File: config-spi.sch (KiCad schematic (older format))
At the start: 45 parts, among them J1 61300611121, U1 XC7K70T-FBG484, U3 S25FL128SAGNFI000

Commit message: Add Xilinx Platfom Cable JTAG interface
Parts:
- removed J1: 61300611121, lpddr4-test-board-footprints:61300611121, symbol lpddr4-test-board:61300611121
- removed R38, R39, R40, R41: R_100R_0402, lpddr4-test-board-footprints:0402-res, symbol lpddr4-test-board:R_100R_0402
- removed Z1, Z2, Z3, Z4: MMSZ5231B-7-F, lpddr4-test-board-footprints:SOD-123, symbol lpddr4-test-board:MMSZ5231B-7-F
- added D?: TPD6E05U06, antmicro-footprints:TPD6E05U06, symbol antmicroTVSDiodes:TPD6E05U06
- added J?: 0878311420, antmicro-footprints:PinHeader_2x7_P2mm_Drill1mm, symbol antmicroRectangularConnectorsHeadersMalePins:0878311420
- added TP?: TP_SMD1MM, lpddr4-test-board-footprints:Testpoint_smd_1mm, symbol lpddr4-test-board:TP_SMD1MM
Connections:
- net labels added: SRST_RDYN
- net labels removed: TCK, TDI_FPGA, TDO_FPGA, TMS
- wire segments 148 -> 149
- no-connect marks 1 -> 2
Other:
- note added: "Compatible with Xilinx Platform Cable"
- note added: "TODO: check this pin connection to FPGA"
- moved on the sheet: J?

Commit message: Add debug configuration resistors
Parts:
- removed JP1: MC-HVT1-S02-G, lpddr4-test-board-footprints:PinHeader_1x2_P1.27mm_Drill.7mm, symbol lpddr4-test-board:MC-HVT1-S02-G
- removed R29, R35: R_1k_0402, lpddr4-test-board-footprints:0402-res, symbol lpddr4-test-board:R_1k_0402
- removed TP?: TP_SMD1MM, lpddr4-test-board-footprints:Testpoint_smd_1mm, symbol lpddr4-test-board:TP_SMD1MM
- added R? (x5): R_1k_0402, lpddr4-test-board-footprints:0402-res, symbol lpddr4-test-board:R_1k_0402
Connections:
- net labels removed: SRST_RDYN
- wire segments 149 -> 151
- no-connect marks 2 -> 3
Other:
- note added: "Config. mode\nMaster Serial\nMaster SPI\nMaster BPI\nMaster SelectMAP\nJTAG\nSlave SelectMAP\nSlave Serial"
- note added: "Debug configuration"
- note added: "For details, see UG470 p. 21"
- note added: "MODE[2:0]\n000\n001\n010\n100\n101\n110\n111"
- note added: "Reference: UG470"
- moved on the sheet: R25

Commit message: Library cleanup, add RGMII layout
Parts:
- D4: renamed from D?; footprint antmicro-footprints:TPD6E05U06 -> lpddr4-test-board-footprints:TPD6E05U06; symbol antmicroTVSDiodes:TPD6E05U06 -> lpddr4-test-board:TPD6E05U06
- J1: renamed from J?; footprint antmicro-footprints:PinHeader_2x7_P2mm_Drill1mm -> lpddr4-test-board-footprints:PinHeader_2x7_P2mm_Drill1mm; symbol antmicroRectangularConnectorsHeadersMalePins:0878311420 -> lpddr4-test-board:0878311420
- gave numbers to parts that had none: 11
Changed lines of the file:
@@
 	11000 3700 11725 3700
 $Comp
-L lpddr4-test-board:R_200R_0402 R?
+L lpddr4-test-board:R_200R_0402 R12
 U 1 1 6AC30A74
 P 7350 8825
-F 0 "R?" H 7150 8875 60  0000 C CNN
+F 0 "R12" H 7150 8875 60  0000 C CNN
 F 1 "R_200R_0402" H 7350 8675 60  0001 C CNN
 F 2 "lpddr4-test-board-footprints:0402-res" H 7550 9025 60  0001 L CNN
@@
 $EndComp
 $Comp
-L lpddr4-test-board:R_200R_0402 R?
+L lpddr4-test-board:R_200R_0402 R11
 U 1 1 6AC310E1
 P 7350 8725
-F 0 "R?" H 7150 8775 60  0000 C CNN
+F 0 "R11" H 7150 8775 60  0000 C CNN
 F 1 "R_200R_0402" H 7350 8575 60  0001 C CNN
 F 2 "lpddr4-test-board-footprints:0402-res" H 7550 8925 60  0001 L CNN
@@
 $EndComp
 $Comp
-L lpddr4-test-board:R_200R_0402 R?
+L lpddr4-test-board:R_200R_0402 R13
 U 1 1 6AC32AC8
 P 7350 8925
-F 0 "R?" H 7150 8975 60  0000 C CNN
+F 0 "R13" H 7150 8975 60  0000 C CNN
 F 1 "R_200R_0402" H 7350 8775 60  0001 C CNN
 F 2 "lpddr4-test-board-footprints:0402-res" H 7550 9125 60  0001 L CNN
@@
 $EndComp
 $Comp
-L lpddr4-test-board:R_200R_0402 R?
+L lpddr4-test-board:R_200R_0402 R14
 U 1 1 6AC32F63
 P 7350 9025
-F 0 "R?" H 7150 9075 60  0000 C CNN
+F 0 "R14" H 7150 9075 60  0000 C CNN
 F 1 "R_200R_0402" H 7350 8875 60  0001 C CNN
 F 2 "lpddr4-test-board-footprints:0402-res" H 7550 9225 60  0001 L CNN
@@
 	6975 8825 7200 8825
 $Comp
-L lpddr4-test-board:61300411121 J?
+L lpddr4-test-board:61300411121 J8
 U 1 1 6AC614B6
 P 9425 8700
-F 0 "J?" V 9300 8675 50  0000 C CNN
+F 0 "J8" V 9300 8675 50  0000 C CNN
 F 1 "61300411121" V 9850 8700 50  0000 C CNN
 F 2 "lpddr4-test-board-footprints:PinHeader_1x4_P2.54mm_Drill1.02mm" H 9625 8900 60  0001 L CNN
@@
 $EndComp
 $Comp
-L lpddr4-test-board:61300611121 J?
+L lpddr4-test-board:61300611121 J5
 U 1 1 6AC62996
 P 6825 8725
-F 0 "J?" V 6700 8700 50  0000 C CNN
+F 0 "J5" V 6700 8700 50  0000 C CNN
 F 1 "61300611121" V 7425 8700 50  0000 C CNN
 F 2 "lpddr4-test-board-footprints:61300611121" H 7025 8925 60  0001 L CNN
@@
 	6975 9225 7250 9225
 $Comp
-L lpddr4-test-board:GND #PWR?
+L lpddr4-test-board:GND #PWR0109
 U 1 1 6B7BF2C0
 P 7250 9400
-F 0 "#PWR?" H 7250 9150 50  0001 C CNN
+F 0 "#PWR0109" H 7250 9150 50  0001 C CNN
 F 1 "GND" H 7255 9227 50  0000 C CNN
 F 2 "" H 7250 9400 50  0001 C CNN
@@
 SPI
 $Comp
-L antmicroRectangularConnectorsHeadersMalePins:0878311420 J?
+L lpddr4-test-board:0878311420 J1
 U 1 1 5FB8277B
 P 2675 8325
-F 0 "J?" H 2675 8850 50  0000 C CNN
+F 0 "J1" H 2675 8850 50  0000 C CNN
 F 1 "0878311420" H 2675 8759 50  0000 C CNN
-F 2 "antmicro-footprints:PinHeader_2x7_P2mm_Drill1mm" H 2875 8525 60  0001 L CNN
+F 2 "lpddr4-test-board-footprints:PinHeader_2x7_P2mm_Drill1mm" H 2875 8525 60  0001 L CNN
 F 3 "https://www.molex.com/pdm_docs/sd/878311420_sd.pdf" H 2875 8625 60  0001 L CNN
 F 4 "0878311420" H 2875 8825 60  0001 L CNN "MPN"
@@
 	2350 8625 2350 8800
 $Comp
-L lpddr4-test-board:GND #PWR?
+L lpddr4-test-board:GND #PWR0110
 U 1 1 5FCE9A21
 P 2350 8800
-F 0 "#PWR?" H 2350 8550 50  0001 C CNN
+F 0 "#PWR0110" H 2350 8550 50  0001 C CNN
 F 1 "GND" H 2355 8627 50  0000 C CNN
 F 2 "" H 2350 8800 50  0001 C CNN
@@
 NoConn ~ 2875 8525
 $Comp
-L antmicroTVSDiodes:TPD6E05U06 D?
+L lpddr4-test-board:TPD6E05U06 D4
 U 1 1 5FCF46CA
 P 3225 9175
-F 0 "D?" V 3445 8497 50  0000 R CNN
+F 0 "D4" V 3445 8497 50  0000 R CNN
 F 1 "TPD6E05U06" V 3354 8497 50  0000 R CNN
-F 2 "antmicro-footprints:TPD6E05U06" H 4425 9425 50  0001 C CNN
+F 2 "lpddr4-test-board-footprints:TPD6E05U06" H 4425 9425 50  0001 C CNN
 F 3 "http://www.ti.com/lit/ds/symlink/tpd6e05u06.pdf" H 4725 9525 50  0001 C CNN
 F 4 "TPD6E05U06RVZR" V 3263 8497 50  0000 R CNN "MPN"
@@
 	3775 8825 4025 8825
 $Comp
-L lpddr4-test-board:GND #PWR?
+L lpddr4-test-board:GND #PWR0111
 U 1 1 5FD74251
 P 4025 8825
-F 0 "#PWR?" H 4025 8575 50  0001 C CNN
+F 0 "#PWR0111" H 4025 8575 50  0001 C CNN
 F 1 "GND" H 4030 8652 50  0000 C CNN
 F 2 "" H 4025 8825 50  0001 C CNN
@@
 Reference: UG470
 $Comp
-L lpddr4-test-board:R_1k_0402 R?
+L lpddr4-test-board:R_1k_0402 R29
 U 1 1 60067D6F
 P 12800 7225
-F 0 "R?" H 12800 7150 60  0000 L CNN
+F 0 "R29" H 12800 7150 60  0000 L CNN
 F 1 "R_1k_0402" H 12800 7075 60  0001 C CNN
 F 2 "lpddr4-test-board-footprints:0402-res" H 13000 7425 60  0001 L CNN
@@
 	12950 7025 13100 7025
 $Comp
-L lpddr4-test-board:GND #PWR?
+L lpddr4-test-board:GND #PWR0113
 U 1 1 60091BBD
 P 13100 7225
-F 0 "#PWR?" H 13100 6975 50  0001 C CNN
+F 0 "#PWR0113" H 13100 6975 50  0001 C CNN
 F 1 "GND" H 13105 7052 50  0000 C CNN
 F 2 "" H 13100 7225 50  0001 C CNN
@@
 	12550 7025 12650 7025
 $Comp
-L lpddr4-test-board:R_1k_0402 R?
+L lpddr4-test-board:R_1k_0402 R35
 U 1 1 600B5E20
 P 12800 7525
-F 0 "R?" H 12800 7450 60  0000 L CNN
+F 0 "R35" H 12800 7450 60  0000 L CNN
 F 1 "R_1k_0402" H 12800 7375 60  0001 C CNN
 F 2 "lpddr4-test-board-footprints:0402-res" H 13000 7725 60  0001 L CNN
@@
 VCC3v3
 $Comp
-L lpddr4-test-board:R_1k_0402 R?
+L lpddr4-test-board:R_1k_0402 R37
 U 1 1 600B5E2A
 P 12800 7725
-F 0 "R?" H 12800 7650 60  0000 L CNN
+F 0 "R37" H 12800 7650 60  0000 L CNN
 F 1 "R_1k_0402" H 12800 7575 60  0001 C CNN
 F 2 "lpddr4-test-board-footprints:0402-res" H 13000 7925 60  0001 L CNN
@@
 	12950 7525 13100 7525
 $Comp
-L lpddr4-test-board:GND #PWR?
+L lpddr4-test-board:GND #PWR0114
 U 1 1 600B5E32
 P 13100 7725
-F 0 "#PWR?" H 13100 7475 50  0001 C CNN
+F 0 "#PWR0114" H 13100 7475 50  0001 C CNN
 F 1 "GND" H 13105 7552 50  0000 C CNN
 F 2 "" H 13100 7725 50  0001 C CNN
@@
 VCC3v3
 $Comp
-L lpddr4-test-board:R_1k_0402 R?
+L lpddr4-test-board:R_1k_0402 R39
 U 1 1 600BDF4C
 P 12800 8200
-F 0 "R?" H 12800 8125 60  0000 L CNN
+F 0 "R39" H 12800 8125 60  0000 L CNN
 F 1 "R_1k_0402" H 12800 8050 60  0001 C CNN
 F 2 "lpddr4-test-board-footprints:0402-res" H 13000 8400 60  0001 L CNN
@@
 	12950 8000 13100 8000
 $Comp
-L lpddr4-test-board:GND #PWR?
+L lpddr4-test-board:GND #PWR0115
 U 1 1 600BDF54
 P 13100 8200
-F 0 "#PWR?" H 13100 7950 50  0001 C CNN
+F 0 "#PWR0115" H 13100 7950 50  0001 C CNN
 F 1 "GND" H 13105 8027 50  0000 C CNN
 F 2 "" H 13100 8200 50  0001 C CNN
@@
 MODE2
 $Comp
-L lpddr4-test-board:R_1k_0402 R?
+L lpddr4-test-board:R_1k_0402 R38
 U 1 1 600D5CDE
 P 12800 8000
-F 0 "R?" H 12800 7925 60  0000 L CNN
+F 0 "R38" H 12800 7925 60  0000 L CNN
 F 1 "R_1k_0402" H 12800 7850 60  0001 C CNN
 F 2 "lpddr4-test-board-footprints:0402-res" H 13000 8200 60  0001 L CNN

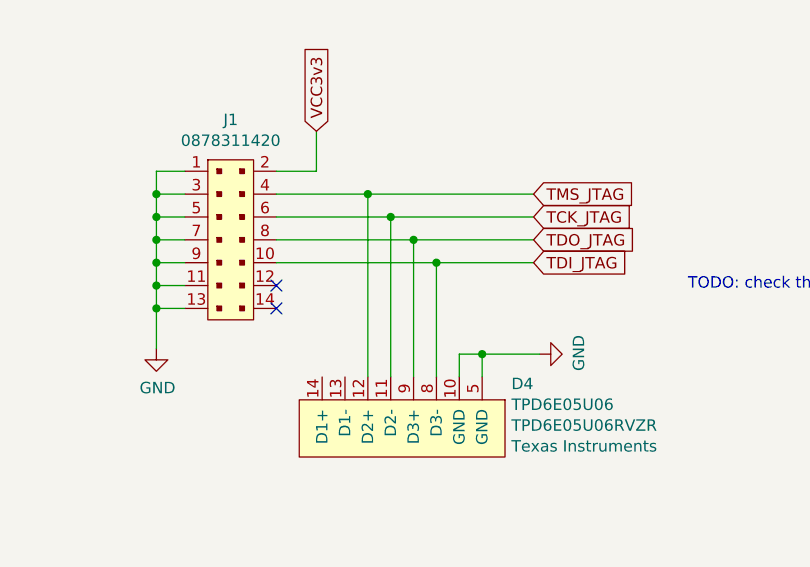
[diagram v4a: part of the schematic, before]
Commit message: Move JTAG connector to the right, add layout
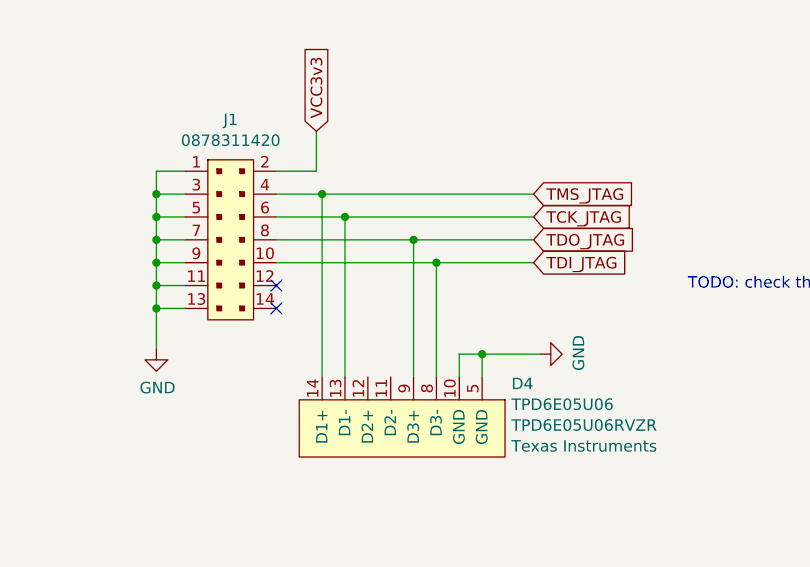
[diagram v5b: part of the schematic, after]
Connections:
- net TCK_JTAG: now also D4.13 (D1-); no longer D4.11 (D2-)
- net TMS_JTAG: now also D4.14 (D1+); no longer D4.12 (D2+)
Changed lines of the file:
@@
 $EndComp
-Wire Wire Line
-	2875 8125 3275 8125
-Wire Wire Line
-	2875 8225 3375 8225
 Wire Wire Line
 	2875 8325 3475 8325
 Wire Wire Line
 	2875 8425 3575 8425
-Wire Wire Line
-	3275 8925 3275 8125
-Connection ~ 3275 8125
-Wire Wire Line
-	3275 8125 4000 8125
-Wire Wire Line
-	3375 8925 3375 8225
-Connection ~ 3375 8225
-Wire Wire Line
-	3375 8225 4000 8225
 Wire Wire Line
 	3475 8925 3475 8325
@@
 Wire Notes Line width 4 style solid
 	13675 6950 14850 6950
+Wire Wire Line
+	3075 8925 3075 8125
+Wire Wire Line
+	2875 8125 3075 8125
+Connection ~ 3075 8125
+Wire Wire Line
+	3075 8125 4000 8125
+Wire Wire Line
+	3175 8925 3175 8225
+Wire Wire Line
+	2875 8225 3175 8225
+Connection ~ 3175 8225
+Wire Wire Line
+	3175 8225 4000 8225
 $EndSCHEMATC

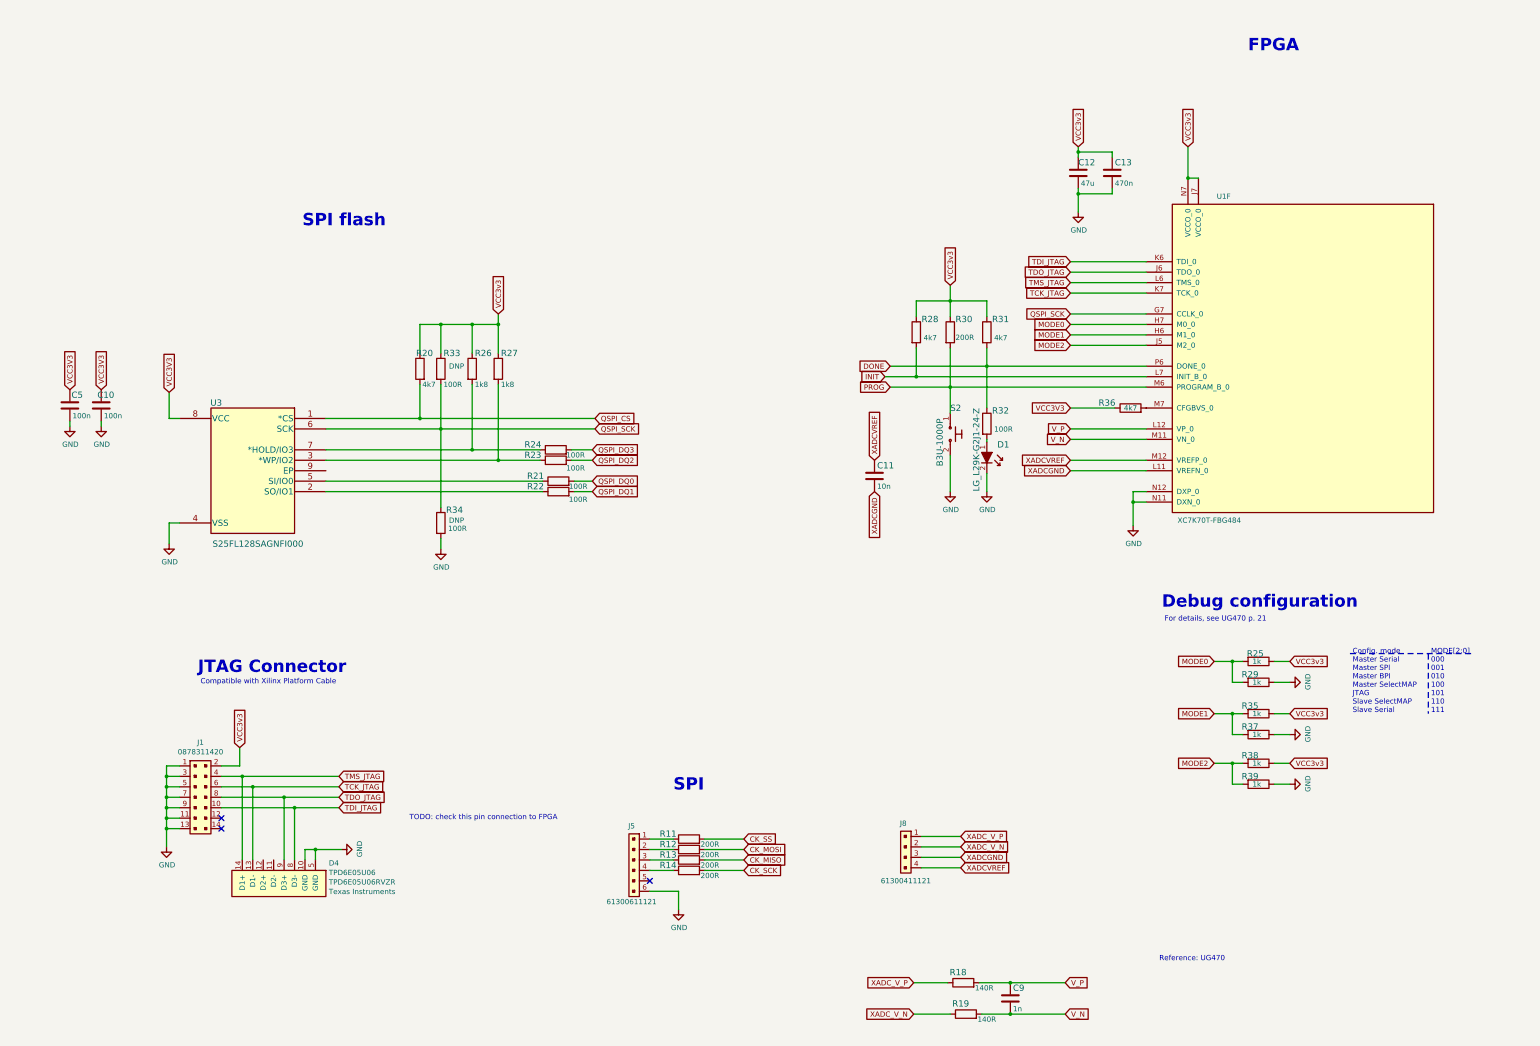
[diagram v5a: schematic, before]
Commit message: Update SPI configuration setup
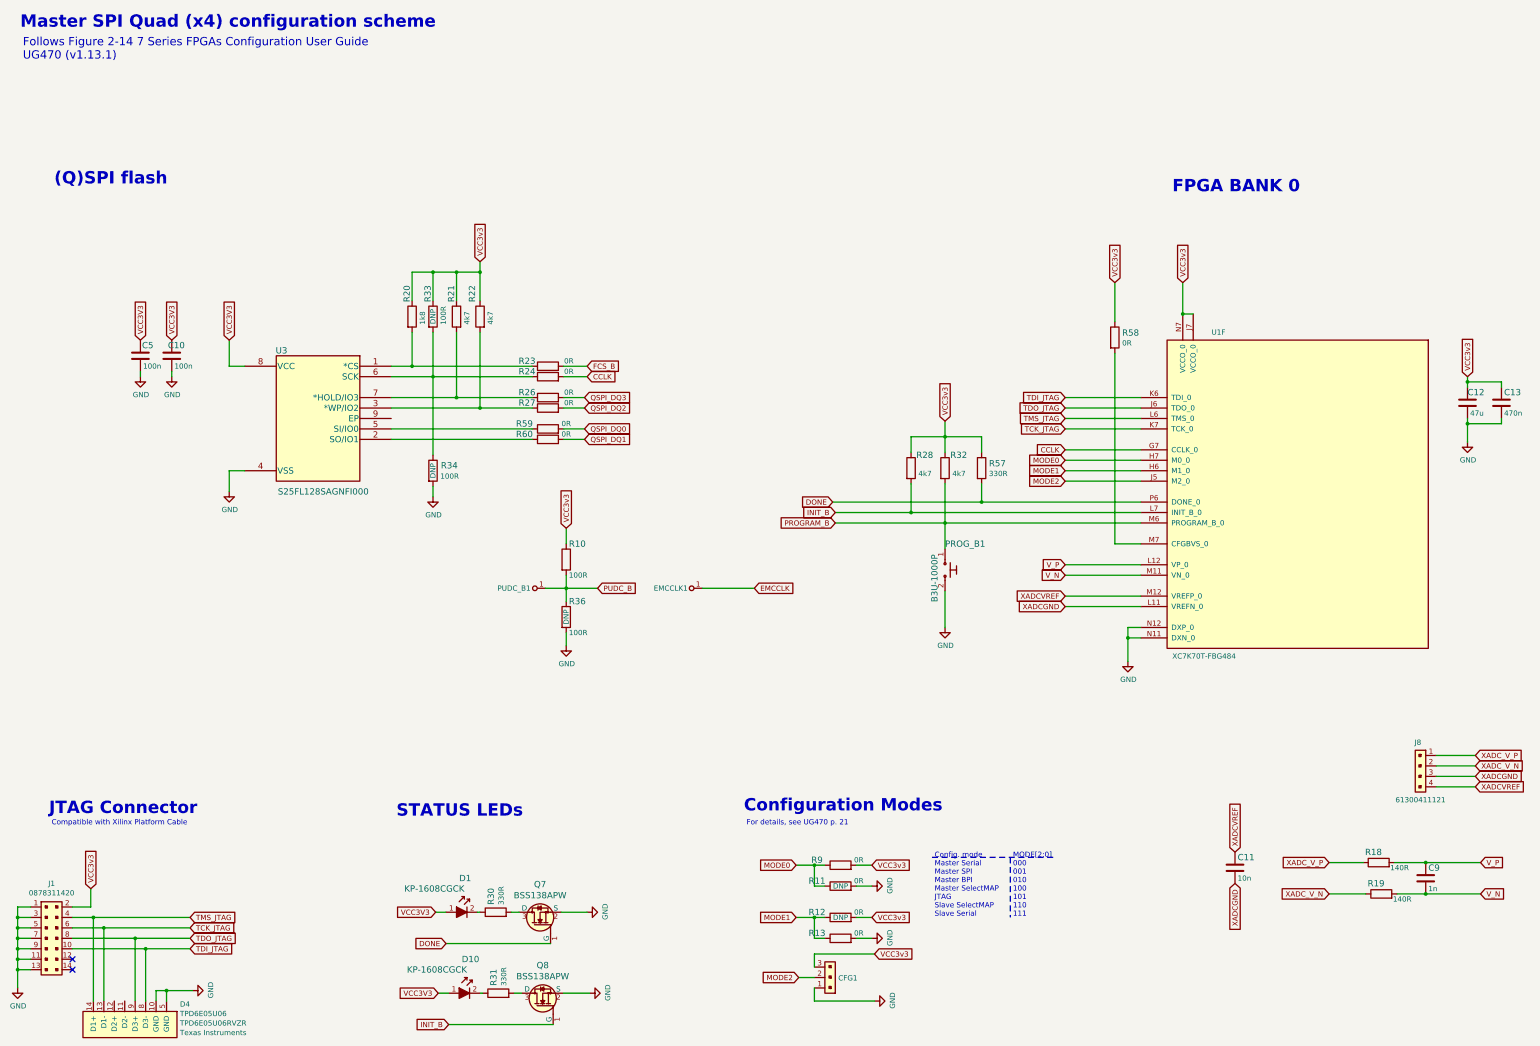
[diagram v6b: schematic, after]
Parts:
- removed D1: LG_L29K-G2J1-24-Z, lpddr4-test-board-footprints:LED_0603, symbol lpddr4-test-board:LG_L29K-G2J1-24-Z
- removed J5: 61300611121, lpddr4-test-board-footprints:61300611121, symbol lpddr4-test-board:61300611121
- removed R11, R12, R13, R14, R30: R_200R_0402, lpddr4-test-board-footprints:0402-res, symbol lpddr4-test-board:R_200R_0402
- removed R20, R31, R36: R_4k7_0402, lpddr4-test-board-footprints:0402-res, symbol lpddr4-test-board:R_4k7_0402
- removed R21, R22, R23, R24, R32: R_100R_0402, lpddr4-test-board-footprints:0402-res, symbol lpddr4-test-board:R_100R_0402
- removed R25, R29, R35, R37, R38, R39: R_1k_0402, lpddr4-test-board-footprints:0402-res, symbol lpddr4-test-board:R_1k_0402
- removed R26, R27: R_1k8_0603, lpddr4-test-board-footprints:0603-res, symbol lpddr4-test-board:R_1k8_0603
- added CFG1: 62000311121, antmicro-footprints:62000311121, symbol antmicroRectangularConnectorsHeadersMalePins:62000311121
- added D1, D10: KP-1608CGCK, lpddr4-test-board-footprints:LED_0603, symbol lpddr4-test-board:KP-1608CGCK
- added EMCCLK1, PUDC_B1: test, symbol antmicroTestPoints:test
- added Q7, Q8: BSS138APW, antmicro-footprints:SC70-3, symbol antmicroTransistorsFETsMOSFETsSingle:BSS138APW
- added R10, R36: R_100R_0402, lpddr4-test-board-footprints:0402-res, symbol lpddr4-test-board:R_100R_0402
- added R11, R12, R13, R23, R24, R26, R27, R58, R59, R60, R9: R_0R_0402, antmicro-footprints:0402-res, symbol antmicroResistors0402:R_0R_0402
- added R20: R_1k8_0603, lpddr4-test-board-footprints:0603-res, symbol lpddr4-test-board:R_1k8_0603
- added R21, R22, R32: R_4k7_0402, lpddr4-test-board-footprints:0402-res, symbol lpddr4-test-board:R_4k7_0402
- added R30, R31: R_330R_0402, lpddr4-test-board-footprints:0402-res, symbol lpddr4-test-board:R_330R_0402
- added R57: R_330R_0402, antmicro-footprints:0402-res, symbol antmicroResistors0402:R_330R_0402
- R33, R34: DNP (none) -> DNP; Populate DNP -> (none)
- renumbered S2 to PROG_B1
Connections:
- net DONE: now also Q7.1 (G), R57.2
- net GND: now also CFG1.1, Q7.2 (S), Q8.2 (S), R11.2, R13.2, R36.2
- net MODE0: now also R11.1, R9.1
- net MODE1: now also R12.1, R13.1
- net MODE2: now also CFG1.2
- net QSPI_DQ0: now also R59.2
- net QSPI_DQ1: now also R60.2
- net QSPI_DQ2: now also R27.2
- net QSPI_DQ3: now also R26.2
- net VCC3V3: now also D1.1, D10.1
- net VCC3v3: now also CFG1.3, R10.1, R12.2, R20.1, R21.1, R22.1, R32.1, R57.1, R58.1, R9.2
- net at U1.M7 (CFGBVS_0): now also R58.2
- net at U3.3 (*WP/IO2): now also R22.2, R27.1
- net at U3.7 (*HOLD/IO3): now also R21.2, R26.1
- net at U3.5 (SI/IO0): now also R59.1
- net at U3.2 (SO/IO1): now also R60.1
- net INIT renamed INIT_B
- net INIT_B: now also Q8.1 (G)
- net PROG renamed PROGRAM_B
- net PROGRAM_B: now also R32.2
- net QSPI_CS: no longer names the net of U3.1 (*CS)
- net QSPI_CS: now also R20.2, R23.1
- net QSPI_SCK: no longer names the net of R33.2, R34.1, U3.6 (SCK)
- net QSPI_SCK: now also R24.1; no longer U1.G7 (CCLK_0)
- new net: D1.2, R30.1
- new net: Q7.3 (D), R30.2
- new net: D10.2, R31.1
- new net: Q8.3 (D), R31.2
- new net CCLK: R24.2, U1.G7 (CCLK_0)
- new net EMCCLK: EMCCLK1.1
- new net FCS_B: R23.2
- new net PUDC_B: PUDC_B1.1, R10.2, R36.1
- no-connect marks 3 -> 2
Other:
- note added: "(Q)SPI flash"
- note added: "Configuration Modes"
- note added: "FPGA BANK 0"
- note added: "Follows Figure 2-14 7 Series FPGAs Configuration User Guide\nUG470 (v1.13.1)"
- note added: "Master SPI Quad (x4) configuration scheme"
- note added: "STATUS LEDs"
- note removed: "Debug configuration"
- note removed: "FPGA"
- note removed: "Reference: UG470"
- note removed: "SPI"
- note removed: "SPI flash"
- note removed: "TODO: check this pin connection to FPGA"
- moved on the sheet: C10, C11, C12, C13, C5, C9, D4, J1, J8, PROG_B1, R18, R19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
